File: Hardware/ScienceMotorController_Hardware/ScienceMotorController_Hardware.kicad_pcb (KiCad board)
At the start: 2 copper layers, 106 parts, among them SW1 SW_Push, SW2 SW_Push, SW3 SW_Push, SW4 SW_Push, U1 TM4C129E_Launchpad, U2 3.3V OKI, U3 5V OKI, U4 VNH5019A_E, U5 VNH5019A_E, U6 VNH5019A_E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

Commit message: PCB High Level Layout
Lacking some major traces such as power
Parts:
- Conn2, Conn3, Conn4, Conn5: moved to B.Cu
- Conn6, Conn7, Conn8, Conn9: footprint MRDT_Connectors:MOLEX_SL_02_Horizontal -> MRDT_Connectors:MOLEX_SL_02_Vertical
- U1: footprint MRDT_Shields:TM4C129E_Launchpad_FULL_THT_BOTTOM -> MRDT_Shields:TM4C129E_Launchpad_FULL_SMD_BOTTOM
- moved Conn7 314.4 mm to (32.9, 55.9)
- moved Conn9 297.9 mm to (32.9, 43.7)
- moved Conn8 269.0 mm to (47.3, 43.7)
- moved Conn6 249.1 mm to (47.3, 55.9)
- moved Conn5 203.7 mm to (128.0, -4.57), turned to 270 degrees
- moved D23 199.6 mm to (131.3, 16.4), turned to 270 degrees
- moved R29 195.1 mm to (73.4, 42.4)
- moved R55 190.3 mm to (131.3, 20.9), turned to 90 degrees
- moved D22 185.6 mm to (108.9, 16.4), turned to 270 degrees
- moved SW1 184.3 mm to (81.5, 40.9)
- moved R54 177.3 mm to (108.9, 20.8), turned to 90 degrees
- moved R31 172.7 mm to (73.4, 52.8)
- moved R30 170.9 mm to (91.7, 42.4)
- moved U7 169.2 mm to (120.1, 12.7), turned to 90 degrees
- moved SW3 162.9 mm to (81.5, 51.3)
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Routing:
- net +12VA: track 0.00 -> 114.0 mm, vias 0 -> 200
- net +12L: track 0.00 -> 46.6 mm
- net +5VL: track 0.00 -> 38.0 mm, vias 0 -> 8
- net +3V3: track 0.00 -> 32.2 mm
- net M4_OUT_B: track 0.00 -> 31.8 mm, vias 0 -> 30
- net M1_OUT_B: track 0.00 -> 31.8 mm, vias 0 -> 30
- net M3_OUT_B: track 0.00 -> 31.8 mm, vias 0 -> 30
- net M2_OUT_B: track 0.00 -> 31.8 mm, vias 0 -> 30
- net M3_OUT_A: track 0.00 -> 31.7 mm, vias 0 -> 30
- net M1_OUT_A: track 0.00 -> 31.7 mm, vias 0 -> 30
- net M4_OUT_A: track 0.00 -> 31.7 mm, vias 0 -> 30
- net M2_OUT_A: track 0.00 -> 31.7 mm, vias 0 -> 30
- net GND: track 0.00 -> 22.2 mm, vias 0 -> 7
- net Net-(R18-Pad2): track 0.00 -> 16.1 mm
- net Net-(R4-Pad2): track 0.00 -> 16.1 mm
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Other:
- board outline added: 124.5 x 117.6 mm

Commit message: Went Overboard on Traces
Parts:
- moved Conn8 79.5 mm to (60.3, 122.2)
- moved D3 73.5 mm to (109.7, 134.1)
- moved R35 73.5 mm to (116.3, 134.1)
- moved Conn9 71.7 mm to (60.3, 110.0)
- moved Conn1 71.0 mm to (161.0, 95.5)
- moved C1 67.5 mm to (124.2, 119.6)
- moved C2 67.5 mm to (128.5, 119.6)
- moved C3 67.5 mm to (134.6, 119.6)
- moved C7 67.5 mm to (102.5, 100.6)
- moved Conn4 67.5 mm to (114.2, 61.7)
- moved Conn5 67.5 mm to (141.0, 61.7)
- moved D10 67.5 mm to (82.8, 134.1)
- moved D11 67.5 mm to (82.8, 137.2)
- moved D13 67.5 mm to (96.3, 131.1)
- moved D14 67.5 mm to (96.3, 134.1)
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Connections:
- U1 pad +3V3': (no net) -> +3V3
- U1 pad +5V': (no net) -> Net-(U1-Pad+5V')
- U1 pad Rese': (no net) -> Net-(U1-PadRese')
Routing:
- net +5VL: track 38.0 -> 169.3 mm, vias 8 -> 9
- net +12VA: track 114.0 -> 187.1 mm, vias 200 -> 202
- net GND: track 22.2 -> 85.9 mm, vias 7 -> 15
- net M2_PWM: track 0.00 -> 57.9 mm, vias 0 -> 1
- net M4_PWM: track 0.00 -> 40.1 mm, vias 0 -> 1
- net LS_2: track 0.00 -> 36.8 mm
- net LS_4: track 0.00 -> 35.8 mm
- net M2_IN_B: track 0.00 -> 32.1 mm, vias 0 -> 1
- net M2_CS: track 3.05 -> 34.0 mm, vias 0 -> 1
- net M3_IN_A: track 0.00 -> 24.5 mm, vias 0 -> 1
- net SW_IND_4: track 0.00 -> 20.9 mm
- net MSW_3: track 10.9 -> 31.0 mm
- net LS_3: track 0.00 -> 20.0 mm
- net LS_1: track 0.00 -> 20.0 mm
- net M1_CS: track 3.05 -> 22.4 mm, vias 0 -> 1
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- added copper zone on B.Cu, net +12VA
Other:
- board size 124.5 x 117.6 mm -> 124.5 x 104.9 mm
- board text added: "Limit Switch 1"
- board text added: "Limit Switch 2"
- board text added: "Limit Switch 3"
- board text added: "Limit Switch 4"
- board text added: "Software 1"
- board text added: "Software 2"
- board text added: "Software 3"
- board text added: "Software 4"

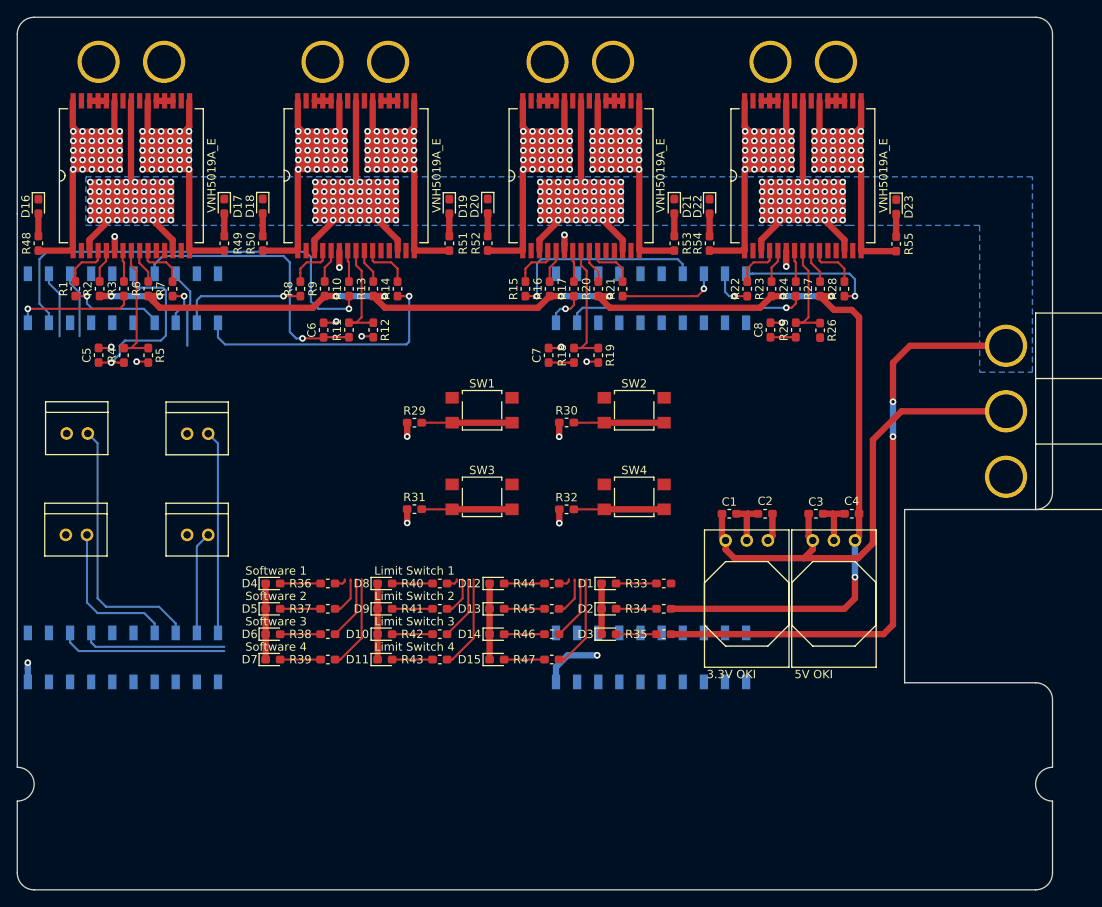
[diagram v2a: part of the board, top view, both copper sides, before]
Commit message: Almost All Traces, Ground and 3V3 Polygons
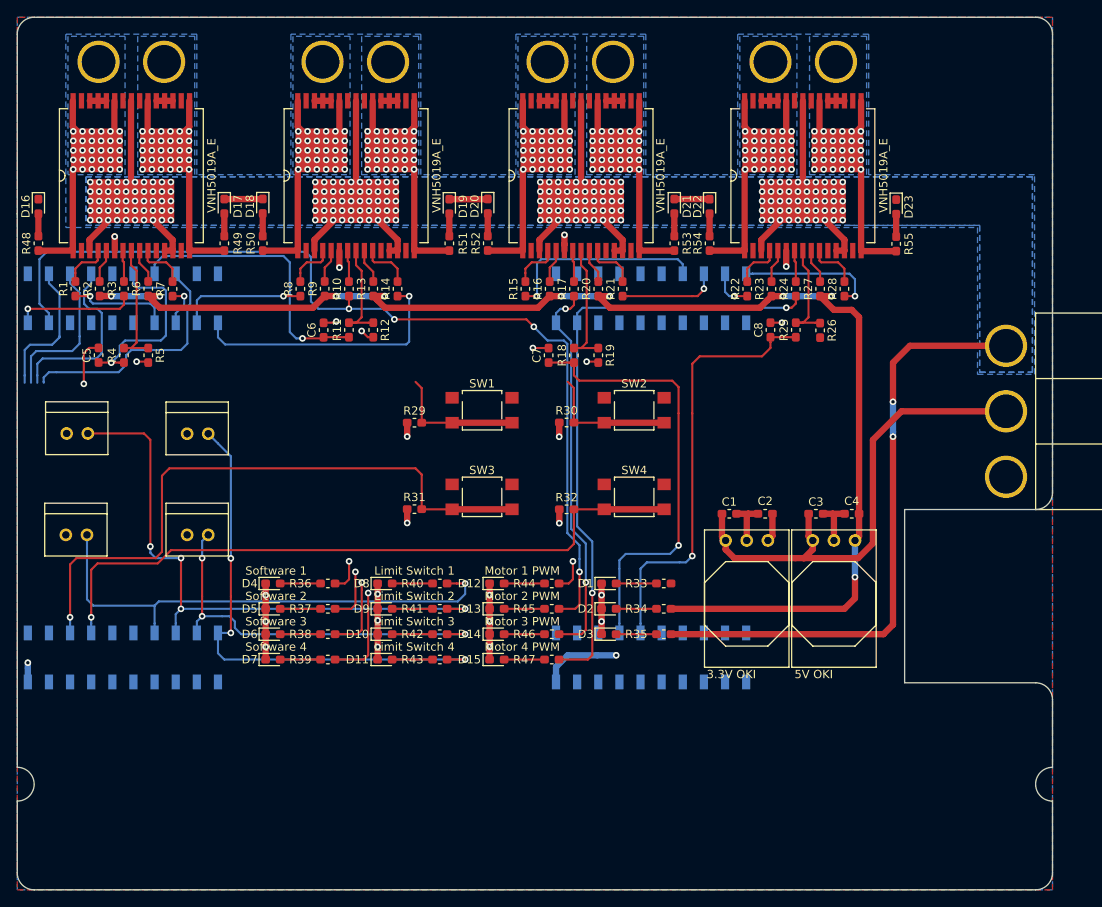
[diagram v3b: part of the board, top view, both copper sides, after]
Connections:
- U4 pad 12: Net-(U4-Pad12) -> +12VA
- U5 pad 12: Net-(U5-Pad12) -> +12VA
- U6 pad 12: Net-(U6-Pad12) -> +12VA
- U7 pad 12: Net-(U7-Pad12) -> +12VA
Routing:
- net M2_PWM: track 57.9 -> 115.8 mm, vias 1 -> 4
- net MSW_4: track 28.2 -> 81.9 mm, vias 0 -> 1
- net M3_CS: track 3.05 -> 53.4 mm, vias 0 -> 1
- net M4_CS: track 3.05 -> 52.2 mm, vias 0 -> 1
- net MSW_3: track 31.0 -> 76.0 mm, vias 0 -> 1
- net LS_1: track 20.0 -> 60.8 mm, vias 0 -> 1
- net LS_2: track 36.8 -> 71.0 mm, vias 0 -> 4
- net M3_PWM: track 12.4 -> 46.6 mm, vias 1 -> 2
- net M4_PWM: track 40.1 -> 73.7 mm, vias 1 -> 2
- net LS_3: track 20.0 -> 47.7 mm, vias 0 -> 3
- net LS_4: track 35.8 -> 61.3 mm, vias 0 -> 3
- net SW_IND_3: track 7.66 -> 31.1 mm, vias 0 -> 1
- net SW_IND_4: track 20.9 -> 41.2 mm, vias 0 -> 1
- net GND: track 85.9 -> 104.1 mm, vias 15 -> 26
- net SW_IND_2: track 12.7 -> 25.1 mm, vias 0 -> 1
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- added copper zone on F.Cu, net +3V3
- added copper zone on B.Cu, net GND
- added copper zone on B.Cu, net M1_OUT_A
- added copper zone on B.Cu, net M1_OUT_B
- added copper zone on B.Cu, net M2_OUT_A
- added copper zone on B.Cu, net M2_OUT_B
- added copper zone on B.Cu, net M3_OUT_A
- added copper zone on B.Cu, net M3_OUT_B
- added copper zone on B.Cu, net M4_OUT_A
- added copper zone on B.Cu, net M4_OUT_B
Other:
- board text added: "Motor 1 PWM"
- board text added: "Motor 2 PWM"
- board text added: "Motor 3 PWM"
- board text added: "Motor 4 PWM"

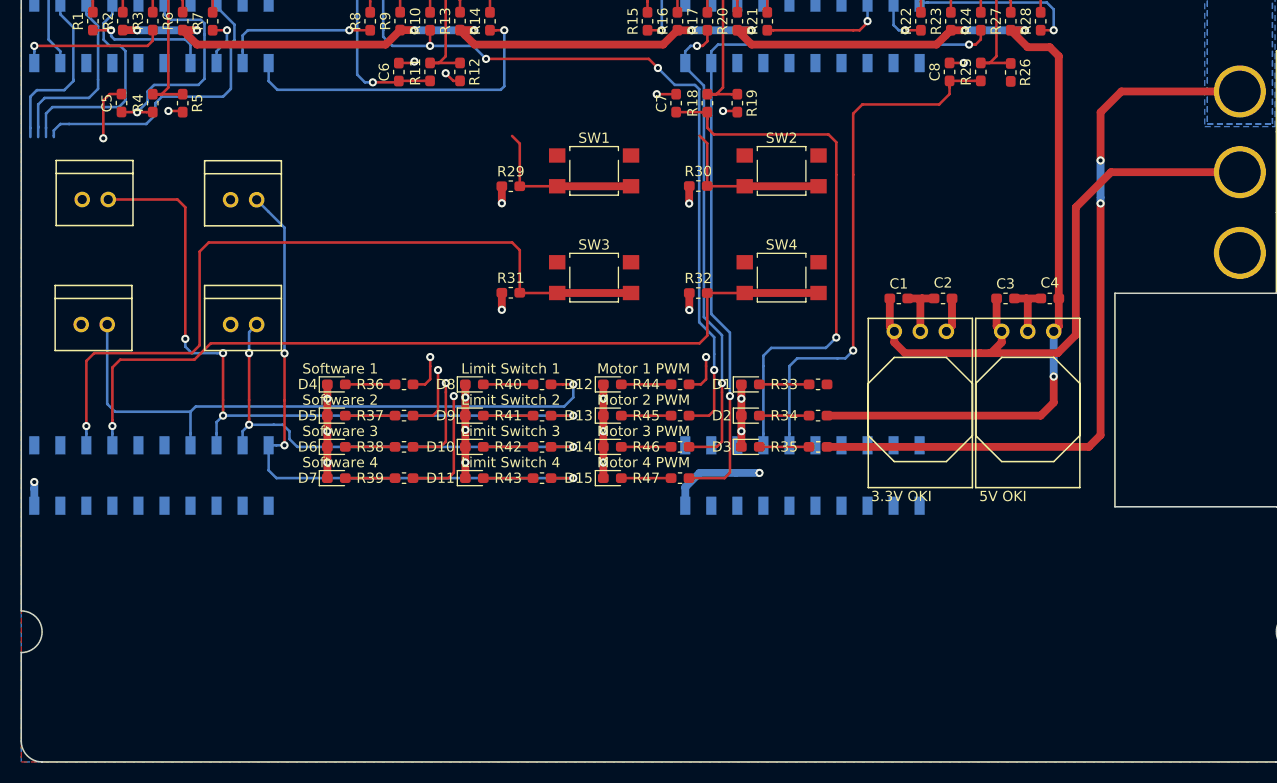
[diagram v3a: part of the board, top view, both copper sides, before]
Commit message: Finally Added Silkscreens
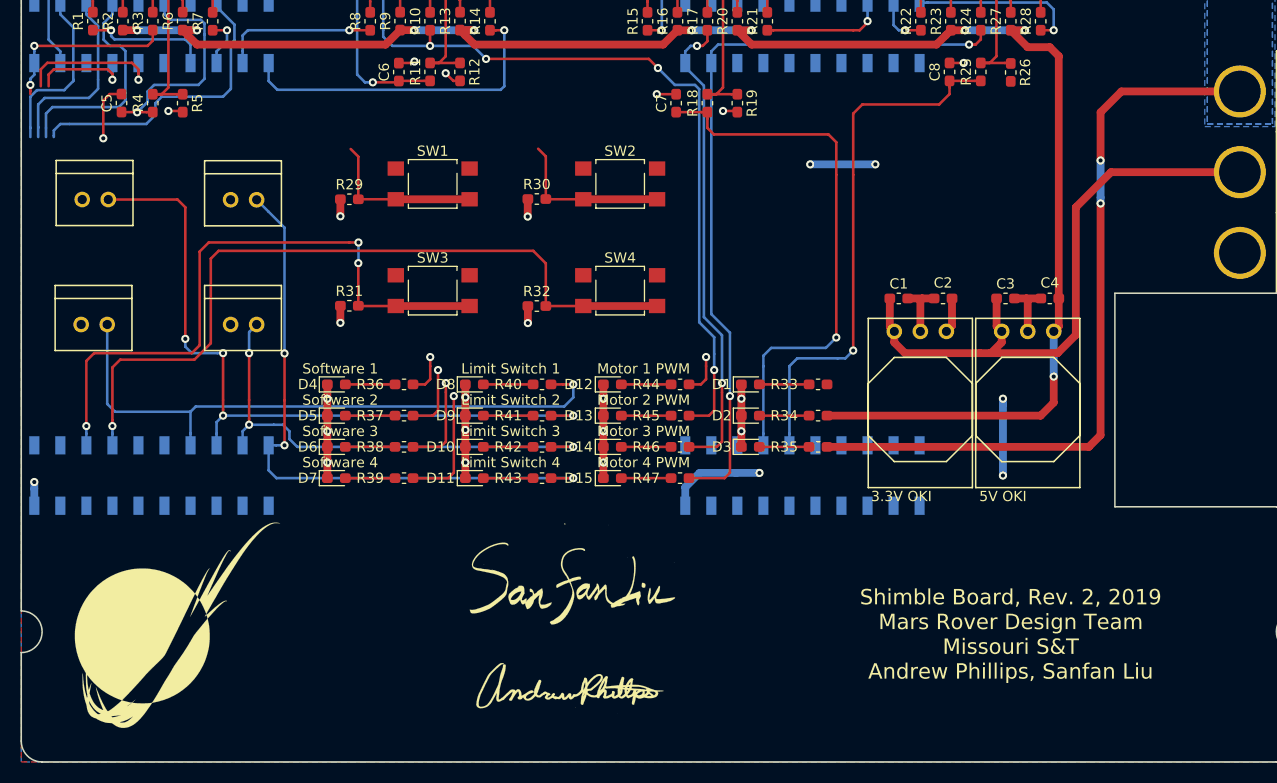
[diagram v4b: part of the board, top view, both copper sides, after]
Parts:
- added G***: LOGO, MRDT_Silkscreens:z_sig_SanfanLiu_sig21.8mmx12.3mm1, F.Cu at (92.1, 147.4)
- added G***: LOGO, MRDT_Silkscreens:z_sig_Andrew_Phillips_Sig_19.7mmx7.7mm, F.Cu at (91.9, 157.7)
- added G***: LOGO, MRDT_Silkscreens:0_MRDT_Logo_20mm, F.Cu at (53.8, 151.5)
- moved R29 15.8 mm to (70.6, 110.0)
- moved R31 15.8 mm to (70.6, 120.3)
- moved SW1 15.8 mm to (78.7, 108.5)
- moved SW3 15.8 mm to (78.7, 118.9)
- moved R30 15.8 mm to (88.9, 109.9)
- moved R32 15.8 mm to (88.9, 120.4)
- moved SW2 15.8 mm to (97.0, 108.5)
- moved SW4 15.8 mm to (97.0, 118.9)
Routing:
- net MSW_2: track 16.1 -> 30.4 mm, vias 0 -> 1
- net MSW_3: track 76.0 -> 61.9 mm, vias 1 -> 3
- net MSW_1: track 16.1 -> 26.0 mm, vias 0 -> 1
- net +3V3: track 15.8 -> 23.3 mm, vias 2 -> 4
- net MSW_4: track 81.9 -> 74.9 mm
- net GND: track 104.1 -> 110.5 mm, vias 26 -> 28
- net M1_PWM: track 18.5 -> 21.7 mm, vias 2 -> 3
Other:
- board text added: "Shimble Board, Rev. 2, 2019 Mars Rover Design Team Missouri S&T Andrew Phillips, Sanfan Liu"

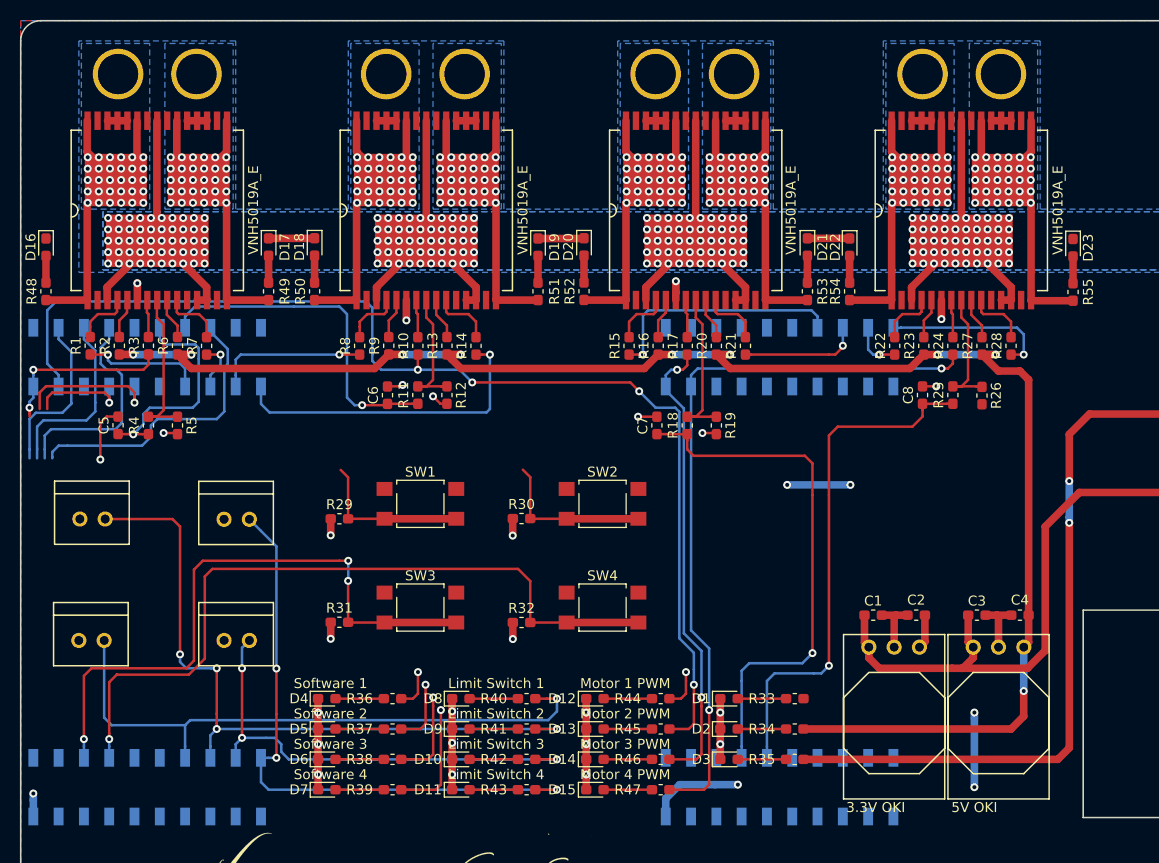
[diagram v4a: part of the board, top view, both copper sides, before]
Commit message: Routed All Traces
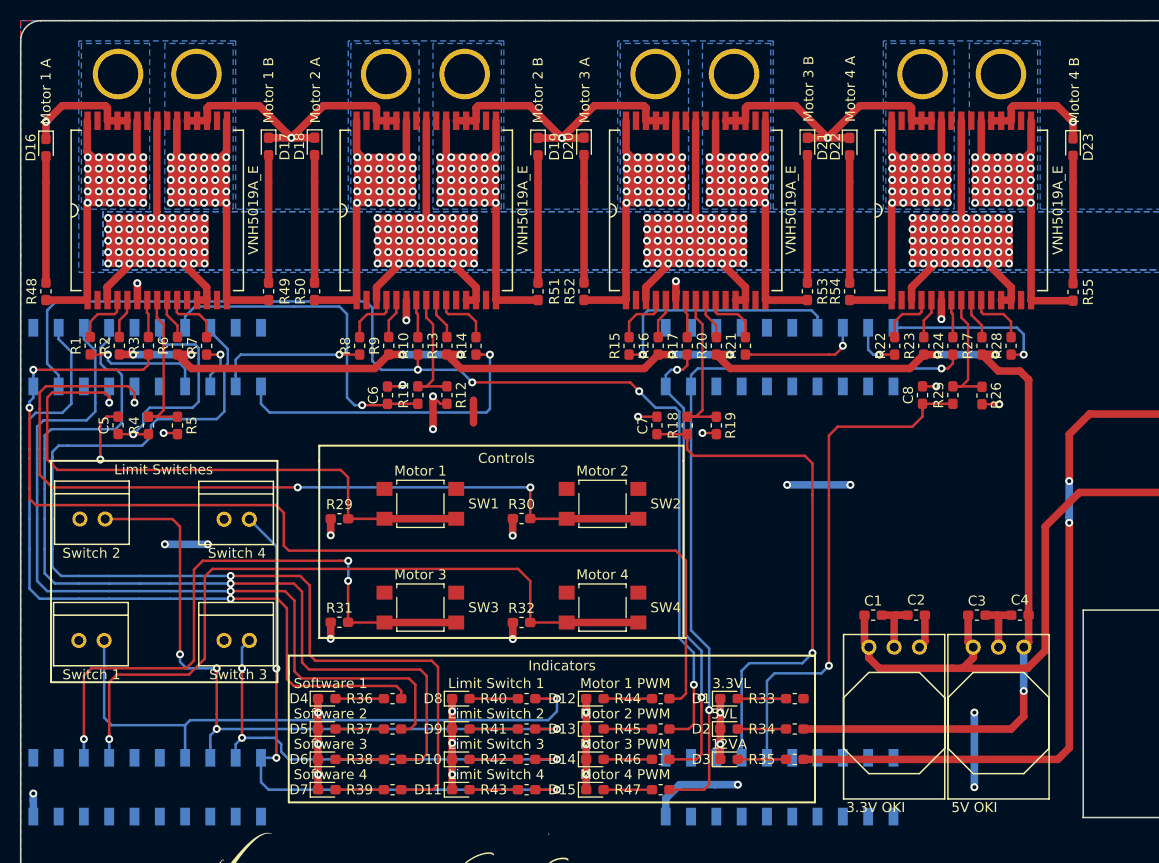
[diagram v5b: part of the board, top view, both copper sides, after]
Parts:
- moved D17 10.1 mm to (63.5, 72.6)
- moved D19 10.1 mm to (90.6, 72.6)
- moved D21 10.1 mm to (117.6, 72.6)
- moved D22 10.1 mm to (121.8, 72.6)
- moved D18 10.1 mm to (68.1, 72.6)
- moved D20 10.1 mm to (95.2, 72.6)
- moved D23 10.1 mm to (144.3, 72.6)
- moved D16 10.00 mm to (41.1, 72.7)
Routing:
- net GND: track 110.5 -> 206.7 mm, vias 28 -> 37
- net M1_PWM: track 21.7 -> 111.5 mm, vias 3 -> 2
- net SW_IND_4: track 41.2 -> 103.2 mm
- net SW_IND_3: track 31.1 -> 90.9 mm
- net SW_IND_2: track 25.1 -> 82.8 mm
- net SW_IND_1: track 21.0 -> 76.5 mm
- net MSW_2: track 30.4 -> 84.7 mm, vias 1 -> 3
- net MSW_1: track 26.0 -> 61.0 mm
- net Net-(D22-Pad2): track 2.70 -> 12.8 mm
- net Net-(D18-Pad2): track 2.70 -> 12.8 mm
- net Net-(D21-Pad2): track 2.70 -> 12.8 mm
- net Net-(D19-Pad2): track 2.70 -> 12.8 mm
- net Net-(D17-Pad2): track 2.70 -> 12.8 mm
- net Net-(D23-Pad2): track 2.70 -> 12.8 mm
- net Net-(D20-Pad2): track 2.70 -> 12.8 mm
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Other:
- board text added: "12VA"
- board text added: "3.3VL"
- board text added: "5VL"
- board text added: "Controls"
- board text added: "Indicators"
- board text added: "Limit Switches"
- board text added: "Motor 1"
- board text added: "Motor 1 A"
- board text added: "Motor 1 B"
- board text added: "Motor 2"
- board text added: "Motor 2 A"
- board text added: "Motor 2 B"
- board text added: "Motor 3"
- board text added: "Motor 3 A"
- board text added: "Motor 3 B"
- board text added: "Motor 4"
- board text added: "Motor 4 A"
- board text added: "Motor 4 B"
- board text added: "Switch 1"
- board text added: "Switch 2"
- board text added: "Switch 3"
- board text added: "Switch 4"
